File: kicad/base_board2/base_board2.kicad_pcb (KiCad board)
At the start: 4 copper layers, 36.7 x 24.1 mm, 25 parts, among them J1 Conn_02x04_Odd_Even, J2 Conn_01x02, SW1 SW_Push, SW2 SW_Push, SW3 SW_Push, SW4 SW_Push, U1 IS31FL3743A, U2 LED matrix 15x10

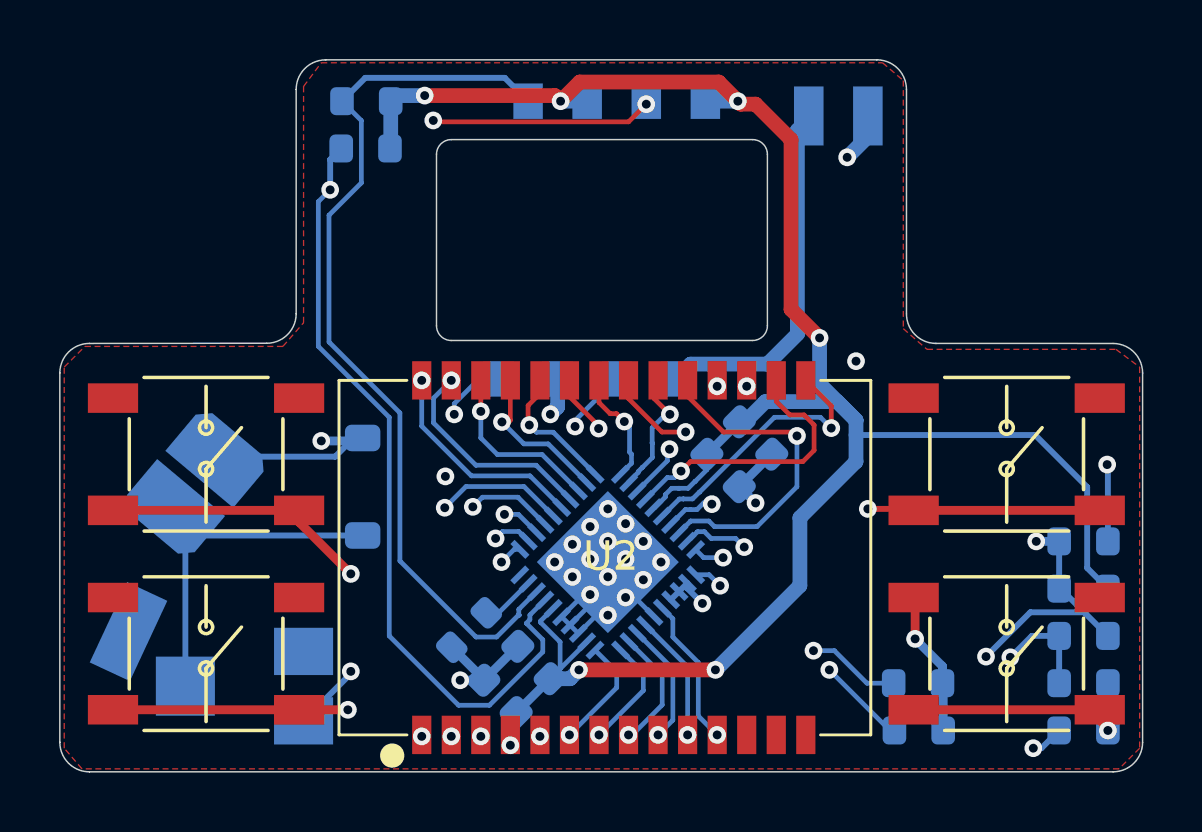
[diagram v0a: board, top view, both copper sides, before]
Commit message: pcbs: improve powering scheme, redesign cartridge; 3dcad: update whole housing
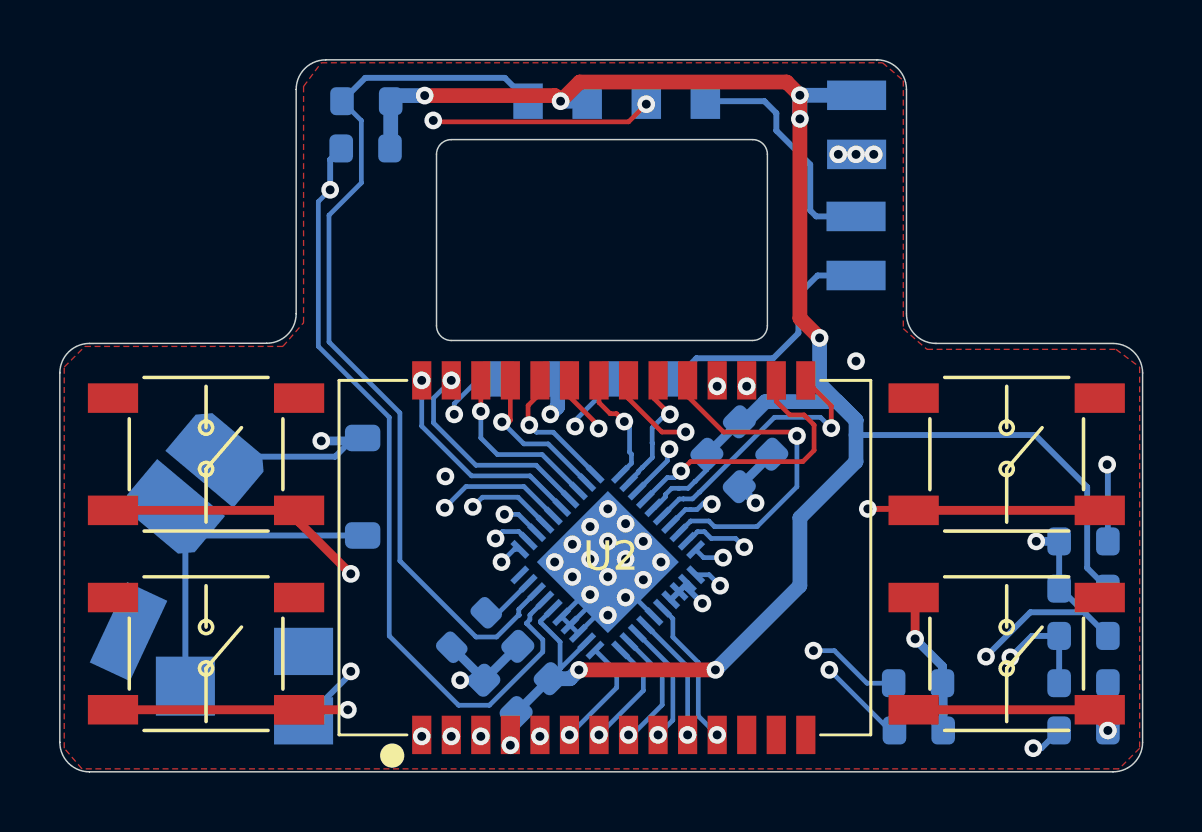
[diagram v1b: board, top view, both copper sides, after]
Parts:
- added J3: Conn_01x02, components:Pads_1x2mm_2x, B.Cu at (132.7, 58.2)
- moved J2 0.69 mm to (132.7, 54.1), turned to -90 degrees
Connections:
- J1 pad 7: VSYS -> PWR_EN1
- J1 pad 8: VCC -> PWR_EN2
- J2 pad 1: VSYS -> VCC
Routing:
- net VSYS: track 12.3 -> 0.00 mm
- net PWR_EN1: track 0.00 -> 8.31 mm
- net PWR_EN2: track 0.00 -> 7.97 mm
- net VCC: track 72.6 -> 75.3 mm, vias 6 -> 7
- net GND: track 44.9 -> 43.2 mm, vias 25 -> 27

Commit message: cartridge pcb panelized; smol fixes to baseboard pcb
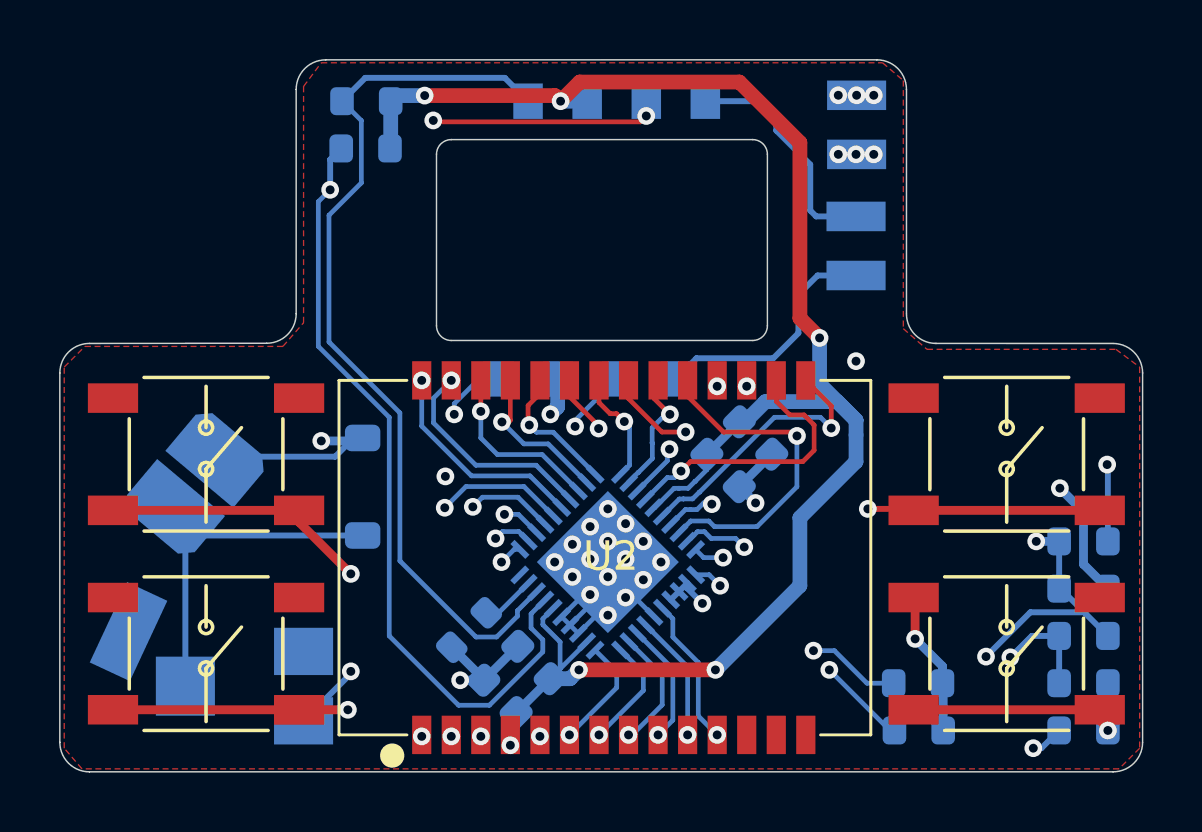
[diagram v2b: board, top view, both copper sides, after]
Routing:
- net VCC: track 75.3 -> 63.3 mm, vias 7 -> 9
- added copper zone on In2.Cu, net VCC

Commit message: 3dcad/housing: fdm & sla variants; kicad/power_supply: add p-down resistor to the MCP1640's EN pin
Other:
- board text added: "V1.2"
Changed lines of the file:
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@@
 			(drillshape 0)
 			(scaleselection 1)
-			(outputdirectory "../../../../../projects/emes/kicad/base_board2/base_board2_gerbers")
+			(outputdirectory "base_board2_gerbers/")
 		)
 	)
@@
 		)
 	)
+	(gr_text "V1.2"
+		(at 139.38 65.56 0)
+		(layer "B.SilkS")
+		(effects
+			(font
+				(size 1 1)
+				(thickness 0.2)
+				(bold yes)
+			)
+			(justify left bottom mirror)
+		)
+	)
